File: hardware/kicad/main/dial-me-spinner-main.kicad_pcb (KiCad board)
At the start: 4 copper layers, 64 x 64 mm, 198 parts, among them J1 LINK, J10 SWD, J20 OLED_ZIF30, J40 MOTOR, Q20 AO3401A, Q21 2N7002, U1 RT9080-33GJ5, U10 MDBT50Q-U1MV2, U11 W25Q128JVSIQ, U2 TPS22917DBVR, U20 TPS61040DBVR, U30 TMAG5273A2QDBVR, U31 LIS2DW12TR, U40 DRV8837DSGR, U41 DRV8837DSGR, U42 DRV5032FADBZR, U43 SN74LV1T34DBVR, Y1 32.768k 9pF

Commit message: WIP: re-placed boards (routing in progress)
Co-Authored-By: Claude Opus 5.5 <noreply@anthropic.com>
Claude-Session: https://claude.ai/code/session_01P3cqdBhxLcWY3sGUVf9LAJ
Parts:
- removed Q20: AO3401A, Package_TO_SOT_SMD:SOT-23
- removed Q21: 2N7002, Package_TO_SOT_SMD:SOT-23
- removed R23: 100k, Resistor_SMD:R_0402_1005Metric
- removed R24: 10k, Resistor_SMD:R_0402_1005Metric
- added C41: 10u, Capacitor_SMD:C_0603_1608Metric, F.Cu at (112.9, 83.7)
- added R59: 1M, Resistor_SMD:R_0402_1005Metric, B.Cu at (121.3, 99.0)
- added U21: TPS22917DBVR, Package_TO_SOT_SMD:SOT-23-6, F.Cu at (113.4, 88.0)
- added U32: TPD4E05U06DQAR, Package_SON:USON-10_2.5x1.0mm_P0.5mm, B.Cu at (104.8, 128.8)
- C37: value 10n -> 1n/50V
- R25: moved to F.Cu
- R57, R58: value 100 -> 470
- moved C37 35.1 mm to (112.9, 85.3)
- moved C38 30.3 mm to (116.8, 86.1)
- moved R25 26.2 mm to (110.5, 89.1), turned to 90 degrees
- moved TP3 9.15 mm to (116.6, 100.4)
- moved D21 8.47 mm to (103.5, 117.3), turned to 0 degrees
- moved TP2 7.20 mm to (119.2, 91.0)
- moved C40 6.00 mm to (107.9, 121.8), turned to 0 degrees
- moved U20 4.45 mm to (108.4, 118.0), turned to 0 degrees
- moved R26 4.29 mm to (107.9, 120.5)
- moved C50 4.04 mm to (103.0, 124.8), turned to 0 degrees
- moved R27 2.64 mm to (105.5, 119.9), turned to 90 degrees
- moved C43 2.44 mm to (123.7, 96.2)
- moved C51 2.23 mm to (104.6, 126.3)
- moved C4 1.98 mm to (116.8, 88.7)
- moved R43 1.61 mm to (121.9, 95.1)
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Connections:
- C37 pad 1: /OLED display & 13 V boost/OLED_PFET_G -> /OLED display & 13 V boost/OLED_LSW_CT
- R41 pad 1: /LED ring/LED_DIN -> /LED ring/LED_DIN_R

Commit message: WIP: re-placed boards with fiducials (routing in progress), --finish clean-up step
Co-Authored-By: Claude Opus 5.5 <noreply@anthropic.com>
Claude-Session: https://claude.ai/code/session_01P3cqdBhxLcWY3sGUVf9LAJ
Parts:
- added FID1: Fiducial_1mm_Mask2mm, Fiducial:Fiducial_1mm_Mask2mm, F.Cu at (113.0, 81.2)
- added FID2: Fiducial_1mm_Mask2mm, Fiducial:Fiducial_1mm_Mask2mm, F.Cu at (77.3, 93.9)
- added FID3: Fiducial_1mm_Mask2mm, Fiducial:Fiducial_1mm_Mask2mm, F.Cu at (105.3, 122.7)
- added FID4: Fiducial_1mm_Mask2mm, Fiducial:Fiducial_1mm_Mask2mm, B.Cu at (124.0, 100.0)
- added FID5: Fiducial_1mm_Mask2mm, Fiducial:Fiducial_1mm_Mask2mm, B.Cu at (76.9, 86.9)
- added FID6: Fiducial_1mm_Mask2mm, Fiducial:Fiducial_1mm_Mask2mm, B.Cu at (92.3, 121.8)
- H1, H2, H3: value MountingHole_2.2mm_M2 -> SPINDLE_M2; footprint MountingHole:MountingHole_2.2mm_M2 -> MountingHole:MountingHole_2.2mm_M2_Pad_Via

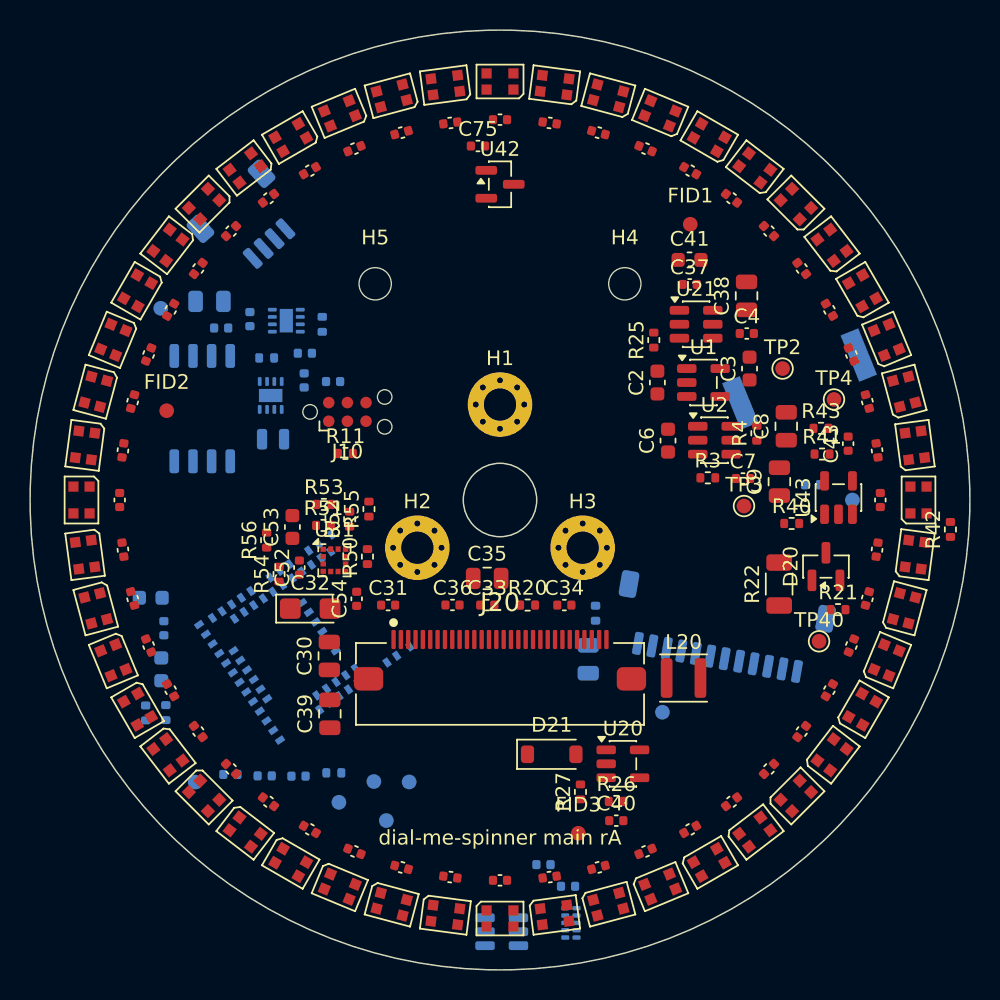
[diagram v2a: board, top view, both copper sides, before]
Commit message: Fix footprint orientation fit (duplicate MP pads), base-board review fixes in progress
- layout.local_map pairs pads by list position, so J1/J3/J2 now face the right way
- base: J2 at θ 222° mouth outward, RT1 on top, BQ25180 off the pack at θ 255°,
  Q1 out of the spoke sector, one boss at r 20 + rib, antenna copper keep-outs
- finish step: zone-aware debris removal, DRC-driven dangling prune, GND stitching
- drc() reports warnings and schematic parity

Co-Authored-By: Claude Opus 5.5 <noreply@anthropic.com>
Claude-Session: https://claude.ai/code/session_01P3cqdBhxLcWY3sGUVf9LAJ
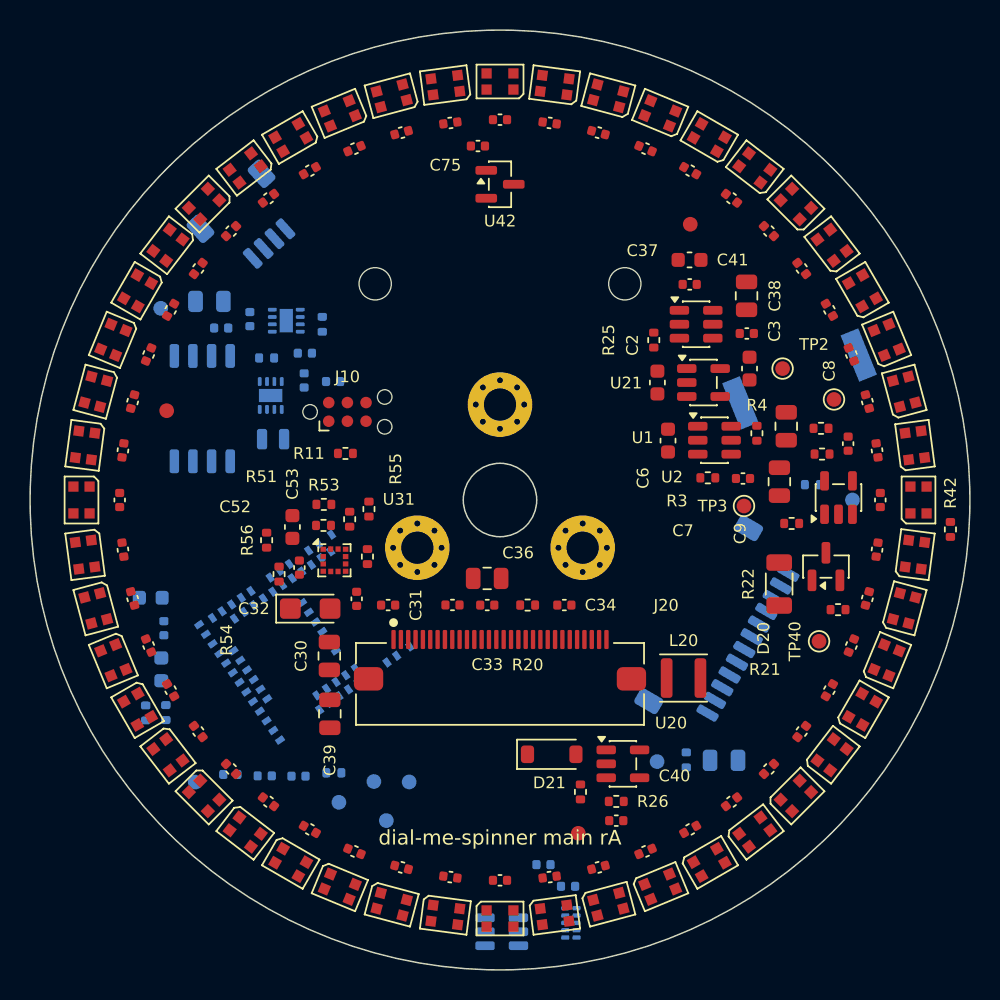
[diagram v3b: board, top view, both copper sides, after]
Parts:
- moved R1 11.7 mm to (112.7, 117.7)
- moved C1 11.5 mm to (115.3, 117.7), turned to 0 degrees
- moved TP1 3.38 mm to (110.7, 117.8)
- turned J1 to 60 degrees

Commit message: Mechanical fit: SH battery connector, module u.FL outward, J1 out of the hub zone
- base J2: JST SH 4-pin side-entry (PH was too tall under the pressed rotor web)
- main: MDBT50Q inner end r >= 8.8 with u.FL facing out; J1 at r 19.5; top r <= 4.6
  kept for the spindle nut; low-profile-only actuator corridor on the bottom
- placer: keep-outs can exempt footprints (low-profile parts)
- enclosure model: coax and battery-lead paths follow the new placement; clash check
  shows only the intended contacts
- docs synced to the earlier late-change list; SPEC updated

Co-Authored-By: Claude Opus 5.5 <noreply@anthropic.com>
Claude-Session: https://claude.ai/code/session_01P3cqdBhxLcWY3sGUVf9LAJ
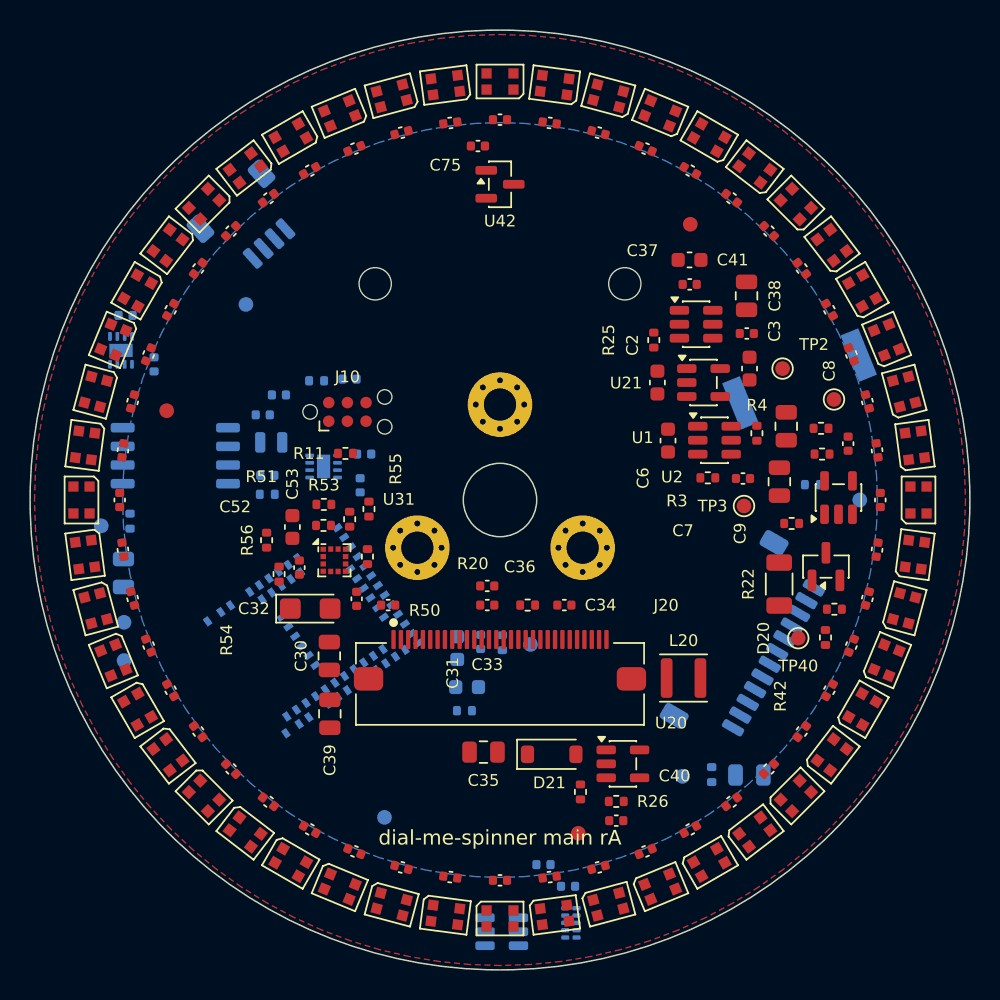
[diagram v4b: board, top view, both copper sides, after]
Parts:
- moved TP13 24.8 mm to (72.8, 101.8)
- moved TP11 24.7 mm to (102.1, 109.8)
- moved C14 23.6 mm to (90.7, 96.9)
- moved R57 23.4 mm to (100.2, 109.7)
- moved C12 22.4 mm to (97.8, 112.7)
- moved R58 21.7 mm to (97.6, 114.3), turned to 0 degrees
- moved C11 21.6 mm to (98.7, 109.7)
- moved TP12 21.1 mm to (74.4, 110.9)
- moved C13 20.8 mm to (90.5, 99.0), turned to 90 degrees
- moved C5 20.6 mm to (84.2, 98.3)
- moved C10 20.2 mm to (97.1, 110.1)
- moved TP10 20.2 mm to (74.4, 108.3)
- moved R2 19.5 mm to (84.2, 99.6)
- moved C74 19.4 mm to (74.4, 105.0), turned to 90 degrees
- moved C73 14.8 mm to (74.5, 87.4)
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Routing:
- added copper zone on B.Cu, net GND
- added copper zone on F.Cu, net GND

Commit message: WIP: SPICE tests and boards in progress
Co-Authored-By: Claude Opus 5.5 <noreply@anthropic.com>
Claude-Session: https://claude.ai/code/session_01P3cqdBhxLcWY3sGUVf9LAJ
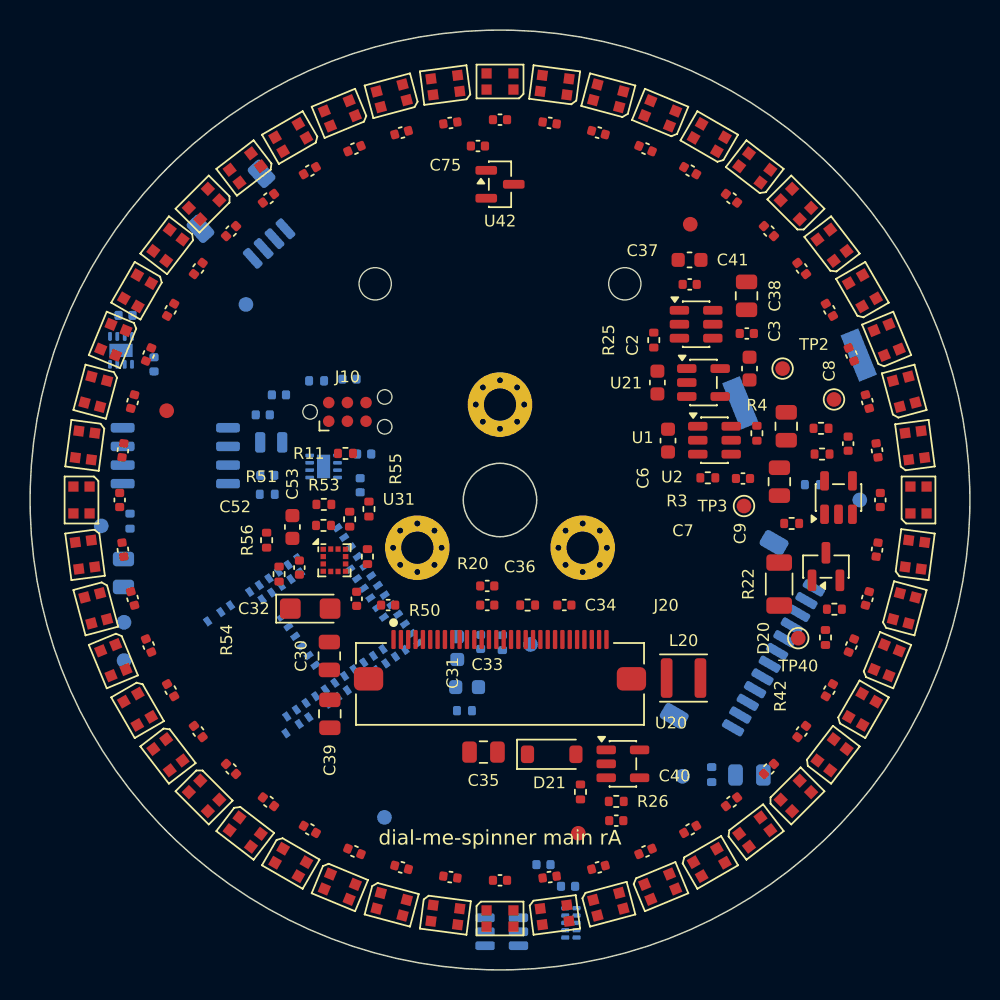
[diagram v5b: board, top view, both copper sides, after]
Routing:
- removed copper zone on B.Cu, net GND
- removed copper zone on F.Cu, net GND
